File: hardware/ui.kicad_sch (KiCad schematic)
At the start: 7 parts, among them SW1 OVERRIDE, SW2 SW_Push, SW3 SW_Push, SW4 SW_Push

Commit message: schematic tidy up, component placement, shielding investigation
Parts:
- removed C40: 1u, Capacitor_SMD:C_0603_1608Metric, symbol Device:C_Small
- removed SW2, SW3: SW_Push, Button_Switch_SMD:SW_SPST_B3U-1000P, symbol Switch:SW_Push
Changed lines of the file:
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@@
   (junction (at 59.69 82.55) (diameter 0) (color 0 0 0 0)
-  )
-  (junction (at 67.31 82.55) (diameter 0) (color 0 0 0 0)
-  )
-  (junction (at 67.31 90.17) (diameter 0) (color 0 0 0 0)
   )
   (wire (pts (xy 67.31 99.06) (xy 73.66 99.06))
     (stroke (width 0) (type default) (color 0 0 0 0))
   )
-  (wire (pts (xy 67.31 91.44) (xy 67.31 90.17))
+  (wire (pts (xy 67.31 88.9) (xy 67.31 91.44))
     (stroke (width 0) (type default) (color 0 0 0 0))
   )
@@
     (stroke (width 0) (type default) (color 0 0 0 0))
   )
-  (wire (pts (xy 74.93 90.17) (xy 67.31 90.17))
-    (stroke (width 0) (type default) (color 0 0 0 0))
-  )
   (wire (pts (xy 59.69 82.55) (xy 59.69 91.44))
-    (stroke (width 0) (type default) (color 0 0 0 0))
-  )
-  (wire (pts (xy 74.93 83.82) (xy 74.93 82.55))
     (stroke (width 0) (type default) (color 0 0 0 0))
   )
@@
     (stroke (width 0) (type default) (color 0 0 0 0))
   )
-  (wire (pts (xy 74.93 82.55) (xy 67.31 82.55))
-    (stroke (width 0) (type default) (color 0 0 0 0))
-  )
-  (wire (pts (xy 67.31 90.17) (xy 67.31 88.9))
-    (stroke (width 0) (type default) (color 0 0 0 0))
-  )
   (wire (pts (xy 59.69 82.55) (xy 67.31 82.55))
-    (stroke (width 0) (type default) (color 0 0 0 0))
-  )
-  (wire (pts (xy 74.93 88.9) (xy 74.93 90.17))
     (stroke (width 0) (type default) (color 0 0 0 0))
   )
@@
   (hierarchical_label "STATUS_LED" (shape input) (at 48.26 99.06 180)
     (effects (font (size 0.8 0.8)) (justify right))
-  )
-  (symbol (lib_id "Switch:SW_Push") (at 135.89 100.33 0) (unit 1)
-    (in_bom yes) (on_board yes) (fields_autoplaced)
-    (property "Reference" "SW2" (id 0) (at 135.89 92.71 0))
-    (property "Value" "SW_Push" (id 1) (at 135.89 95.25 0))
-    (property "Footprint" "Button_Switch_SMD:SW_SPST_B3U-1000P" (id 2) (at 135.89 95.25 0))
-    (property "Datasheet" "~" (id 3) (at 135.89 95.25 0)
-      (effects (font (size 1.27 1.27)) hide)
-    )
-    (pin "1")
-    (pin "2")
   )
   (symbol (lib_id "LED:SK6805") (at 59.69 99.06 0) (unit 1)
@@
     (pin "1")
   )
-  (symbol (lib_id "Device:C_Small") (at 74.93 86.36 0) (unit 1)
-    (in_bom yes) (on_board yes)
-    (property "Reference" "C40" (id 0) (at 77.47 85.09 0)
-      (effects (font (size 0.8 0.8)) (justify left))
-    )
-    (property "Value" "1u" (id 1) (at 77.47 86.36 0)
-      (effects (font (size 0.8 0.8)) (justify left))
-    )
-    (property "Footprint" "Capacitor_SMD:C_0603_1608Metric" (id 2) (at 74.93 86.36 0)
-      (effects (font (size 0.8 0.8)) hide)
-    )
-    (property "Datasheet" "~" (id 3) (at 74.93 86.36 0)
-      (effects (font (size 0.8 0.8)) hide)
-    )
-    (property "Voltage" "15V" (id 4) (at 77.47 87.63 0)
-      (effects (font (size 0.8 0.8)) (justify left))
-    )
-    (pin "1")
-    (pin "2")
-  )
-  (symbol (lib_id "Switch:SW_Push") (at 135.89 76.2 0) (unit 1)
-    (in_bom yes) (on_board yes) (fields_autoplaced)
-    (property "Reference" "SW3" (id 0) (at 135.89 68.58 0))
-    (property "Value" "SW_Push" (id 1) (at 135.89 71.12 0))
-    (property "Footprint" "Button_Switch_SMD:SW_SPST_B3U-1000P" (id 2) (at 135.89 71.12 0))
-    (property "Datasheet" "~" (id 3) (at 135.89 71.12 0)
-      (effects (font (size 1.27 1.27)) hide)
-    )
-    (pin "1")
-    (pin "2")
-  )
   (symbol (lib_id "bt_power:VDD_DISP_3V3") (at 59.69 81.28 0) (unit 1)

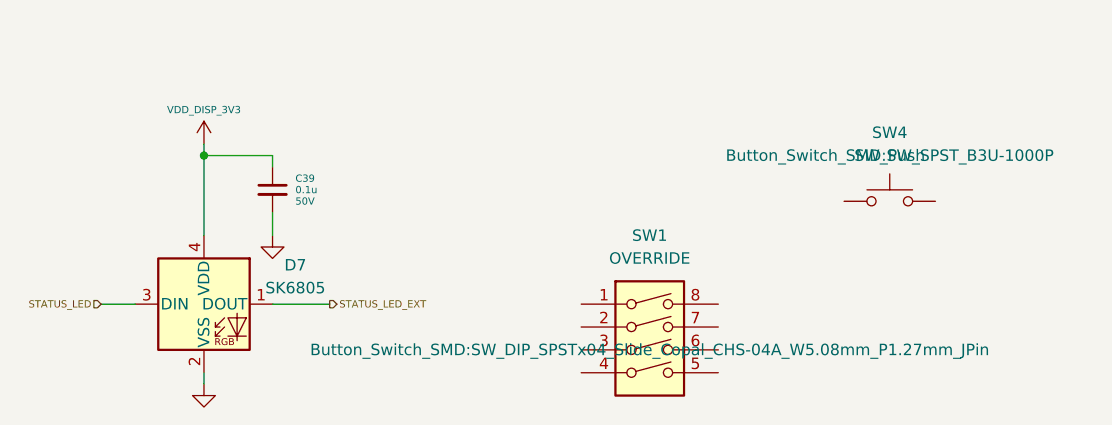
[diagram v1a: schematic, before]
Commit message: screen mock, tweaked layout easier powerplane division
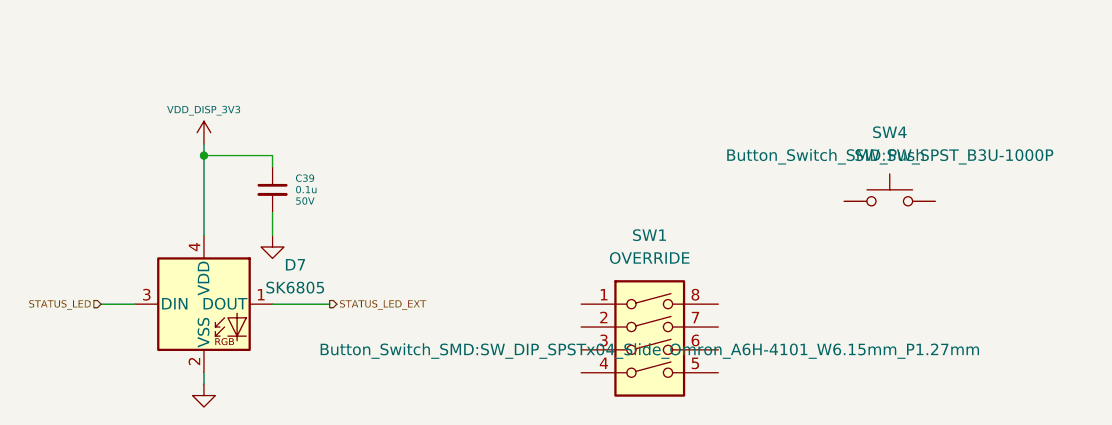
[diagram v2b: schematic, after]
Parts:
- SW1: footprint Button_Switch_SMD:SW_DIP_SPSTx04_Slide_Copal_CHS-04A_W5.08mm_P1.27mm_JPin -> Button_Switch_SMD:SW_DIP_SPSTx04_Slide_Omron_A6H-4101_W6.15mm_P1.27mm
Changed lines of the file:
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@@
     (property "Reference" "SW1" (id 0) (at 109.22 91.44 0))
     (property "Value" "OVERRIDE" (id 1) (at 109.22 93.98 0))
-    (property "Footprint" "Button_Switch_SMD:SW_DIP_SPSTx04_Slide_Copal_CHS-04A_W5.08mm_P1.27mm_JPin" (id 2) (at 109.22 104.14 0))
+    (property "Footprint" "Button_Switch_SMD:SW_DIP_SPSTx04_Slide_Omron_A6H-4101_W6.15mm_P1.27mm" (id 2) (at 109.22 104.14 0))
     (property "Datasheet" "~" (id 3) (at 109.22 104.14 0)
       (effects (font (size 1.27 1.27)) hide)

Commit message: Updates
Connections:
- net VDD_DISP_3V3: no longer names the net of D7.4 (VDD)
- net VDD_DISP_3V3: no longer C39.1
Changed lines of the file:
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@@
 (kicad_sch (version 20211123) (generator eeschema)
   (paper "A4")
-  (junction (at 59.69 82.55) (diameter 0) (color 0 0 0 0)
-  )
   (wire (pts (xy 67.31 99.06) (xy 73.66 99.06))
     (stroke (width 0) (type default) (color 0 0 0 0))
@@
   )
   (wire (pts (xy 59.69 82.55) (xy 59.69 91.44))
-    (stroke (width 0) (type default) (color 0 0 0 0))
-  )
-  (wire (pts (xy 67.31 82.55) (xy 67.31 83.82))
-    (stroke (width 0) (type default) (color 0 0 0 0))
-  )
-  (wire (pts (xy 59.69 81.28) (xy 59.69 82.55))
-    (stroke (width 0) (type default) (color 0 0 0 0))
-  )
-  (wire (pts (xy 59.69 82.55) (xy 67.31 82.55))
     (stroke (width 0) (type default) (color 0 0 0 0))
   )
@@
     )
     (pin "1")
-  )
-  (symbol (lib_id "bt_power:VDD_DISP_3V3") (at 59.69 81.28 0) (unit 1)
-    (in_bom no) (on_board no)
-    (property "Reference" "#U0107" (id 0) (at 60.2234 81.28 0)
-      (effects (font (size 1.27 1.27)) hide)
-    )
-    (property "Value" "VDD_DISP_3V3" (id 1) (at 59.69 77.47 0)
-      (effects (font (size 0.8 0.8)))
-    )
-    (property "Footprint" "" (id 2) (at 60.2234 81.28 0)
-      (effects (font (size 1.27 1.27)) hide)
-    )
-    (property "Datasheet" "" (id 3) (at 60.2234 81.28 0)
-      (effects (font (size 1.27 1.27)) hide)
-    )
-    (pin "1")
